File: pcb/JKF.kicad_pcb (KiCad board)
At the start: 2 copper layers, 77.2 x 50.8 mm, 78 parts, among them J1 Conn_01x10_Socket, J10 Conn_01x02_Socket, J11 Conn_01x02_Socket, J12 Conn_01x02_Socket, J13 Conn_01x02_Socket, J14 Conn_01x02_Socket, J15 Conn_01x02_Socket, J16 Conn_01x02_Socket, J17 Conn_01x02_Socket, J18 Conn_01x02_Socket, J19 Conn_01x02_Socket, J2 Conn_01x02_Pin, J20 Conn_01x02_Socket, J21 Conn_01x02_Socket, J22 Conn_01x02_Socket, J23 Conn_01x02_Socket, J24 Conn_01x02_Socket, J25 Conn_01x02_Socket, J26 Conn_01x02_Socket, J27 Conn_01x02_Socket, J28 Conn_01x02_Socket, J29 Conn_01x02_Socket, J3 Conn_01x10_Socket, J30 Conn_01x02_Socket, J31 Conn_01x02_Socket, J32 Conn_01x02_Socket, J33 Conn_01x02_Socket, J34 Conn_01x02_Socket, J35 Conn_01x02_Socket, J36 Conn_01x02_Socket, J37 Conn_01x02_Socket, J4 Conn_02x02_Counter_Clockwise, J5 Conn_02x02_Counter_Clockwise, J6 Conn_02x02_Counter_Clockwise, J7 Conn_02x02_Counter_Clockwise, J8 Conn_02x02_Counter_Clockwise, J9 Conn_02x02_Counter_Clockwise, U1 4027, U2 4027

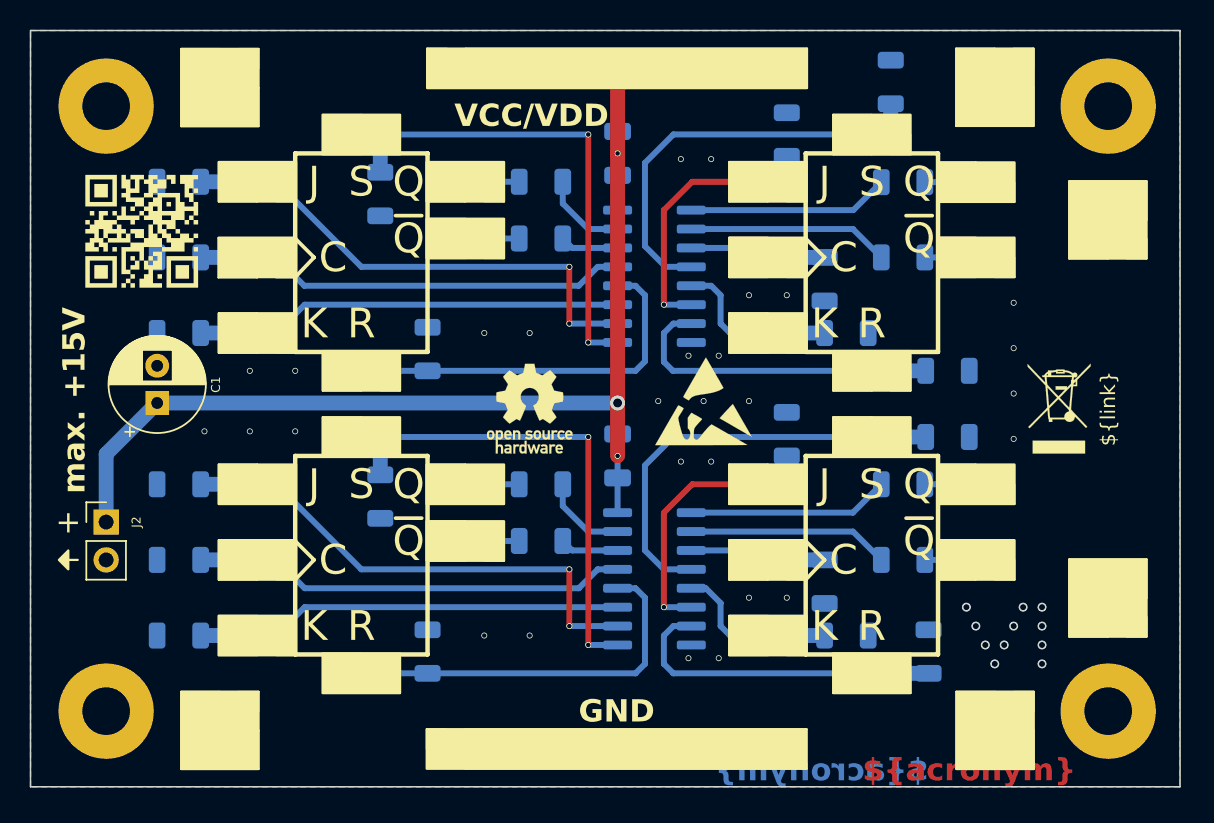
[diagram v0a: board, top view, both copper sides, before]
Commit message: Adapt edge cuts and dimensioning
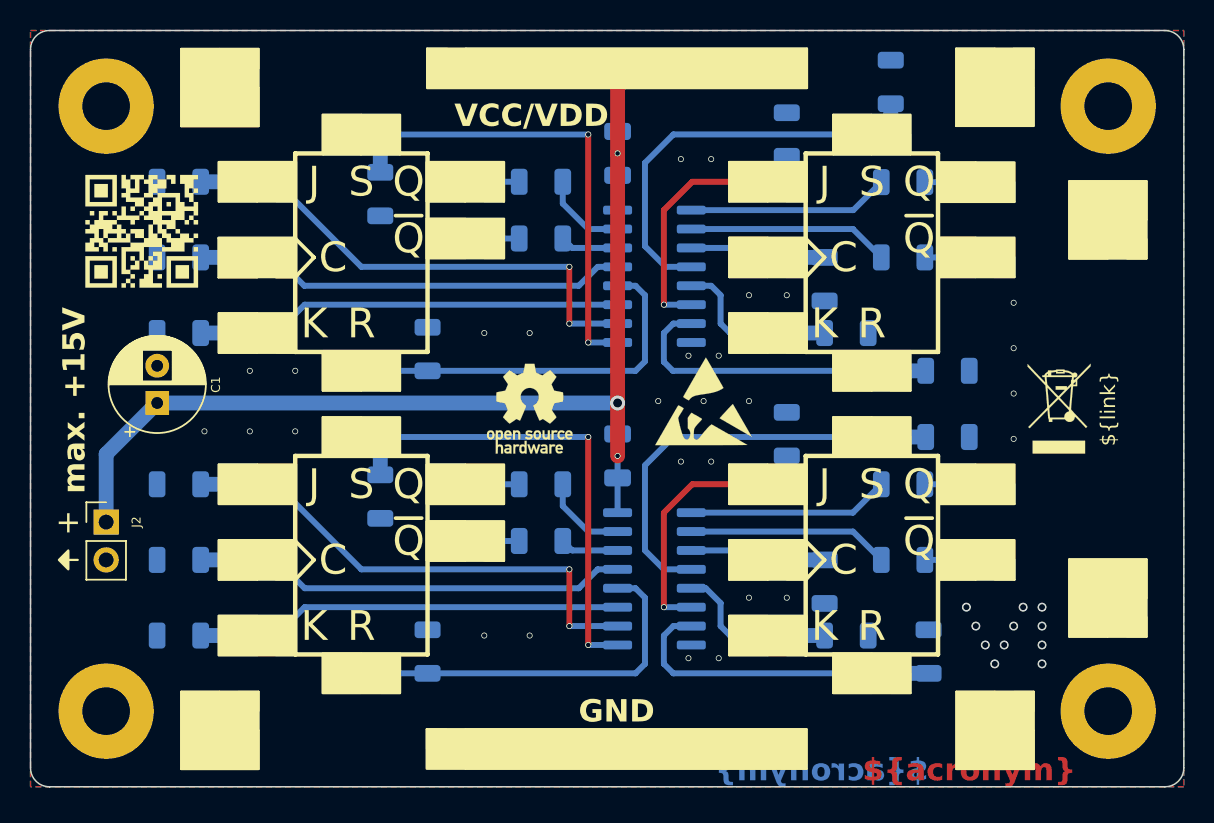
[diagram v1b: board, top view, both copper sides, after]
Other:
- board size 77.2 x 50.8 mm -> 77.5 x 50.8 mm
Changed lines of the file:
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@@
   (gr_rect (start 145.99 105.35) (end 151.19 108.01)
     (stroke (width 0.15) (type solid)) (fill solid) (layer "F.SilkS"))
-  (gr_rect (start 119.38 76.2) (end 196.596 127)
-    (stroke (width 0.1) (type default)) (fill none) (layer "Edge.Cuts"))
+  (gr_line (start 195.58 76.2) (end 120.65 76.2)
+    (stroke (width 0.1) (type default)) (layer "Edge.Cuts"))
+  (gr_line (start 196.85 125.73) (end 196.85 77.47)
+    (stroke (width 0.1) (type default)) (layer "Edge.Cuts"))
+  (gr_line (start 119.38 77.47) (end 119.38 125.73)
+    (stroke (width 0.1) (type default)) (layer "Edge.Cuts"))
+  (gr_arc (start 195.58 76.2) (mid 196.478026 76.571974) (end 196.85 77.47)
+    (stroke (width 0.1) (type default)) (layer "Edge.Cuts"))
+  (gr_arc (start 119.38 77.47) (mid 119.751974 76.571974) (end 120.65 76.2)
+    (stroke (width 0.1) (type default)) (layer "Edge.Cuts"))
+  (gr_line (start 120.65 127) (end 195.58 127)
+    (stroke (width 0.1) (type default)) (layer "Edge.Cuts"))
+  (gr_arc (start 196.85 125.73) (mid 196.478026 126.628026) (end 195.58 127)
+    (stroke (width 0.1) (type default)) (layer "Edge.Cuts"))
+  (gr_arc (start 120.65 127) (mid 119.751974 126.628026) (end 119.38 125.73)
+    (stroke (width 0.1) (type default)) (layer "Edge.Cuts"))
   (gr_text "${acronym}" (at 175.26 126.746) (layer "F.Cu")
     (effects (font (size 1.5 1.5) (thickness 0.3) bold) (justify left bottom))
@@
   (dimension (type aligned) (layer "Dwgs.User")
     (pts (xy 119.38 76.2) (xy 119.38 127))
-    (height 1.27)
-    (gr_text "50.80" (at 116.96 101.6 90) (layer "Dwgs.User")
+    (height 3.81)
+    (gr_text "50.80" (at 114.42 101.6 90) (layer "Dwgs.User")
       (effects (font (size 1 1) (thickness 0.15)))
     )
@@
   )
   (dimension (type aligned) (layer "Dwgs.User")
-    (pts (xy 119.38 76.2) (xy 196.596 76.2))
-    (height -1.27)
-    (gr_text "77.22" (at 157.988 73.78) (layer "Dwgs.User")
+    (pts (xy 119.38 76.2) (xy 196.85 76.2))
+    (height -3.81)
+    (gr_text "77.47" (at 158.115 71.24) (layer "Dwgs.User")
+      (effects (font (size 1 1) (thickness 0.15)))
+    )
+    (format (prefix "") (suffix "") (units 3) (units_format 0) (precision 2))
+    (style (thickness 0.15) (arrow_length 1.27) (text_position_mode 0) (extension_height 0.58642) (extension_offset 0.5) keep_text_aligned)
+  )
+  (dimension (type aligned) (layer "Dwgs.User")
+    (pts (xy 124.46 81.28) (xy 124.46 76.2))
+    (height -6.35)
+    (gr_text "5.08" (at 116.96 78.74 90) (layer "Dwgs.User")
+      (effects (font (size 1 1) (thickness 0.15)))
+    )
+    (format (prefix "") (suffix "") (units 3) (units_format 0) (precision 2))
+    (style (thickness 0.15) (arrow_length 1.27) (text_position_mode 0) (extension_height 0.58642) (extension_offset 0.5) keep_text_aligned)
+  )
+  (dimension (type aligned) (layer "Dwgs.User")
+    (pts (xy 124.46 81.28) (xy 119.38 81.28))
+    (height 6.35)
+    (gr_text "5.08" (at 121.92 73.78) (layer "Dwgs.User")
       (effects (font (size 1 1) (thickness 0.15)))
     )
@@
       (pts
         (xy 119.38 76.2)
-        (xy 196.596 76.2)
-        (xy 196.596 127)
+        (xy 196.85 76.2)
+        (xy 196.85 127)
         (xy 119.38 127)
       )

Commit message: Add reverse polarity protection
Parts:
- added D1: BAT43, Diode_SMD:D_MiniMELF, B.Cu at (139.2, 121.7)
- added D2: BZ5V1, Diode_SMD:D_MiniMELF, B.Cu at (144.5, 123.4)
- added Q1: BUK7880-55A, Package_TO_SOT_SMD:SOT-223-3_TabPin2, B.Cu at (151.8, 119.4)
- added R29: 1k, Resistor_SMD:R_1206_3216Metric, B.Cu at (139.5, 124.0)
- moved R19 13.0 mm to (158.8, 120.8), turned to 90 degrees
- moved R4 2.07 mm to (130.8, 115.4), turned to -90 degrees
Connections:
- J2 pad 2: GND -> Net-(J2-Pin_2)
- J3 pad 1: GND -> Net-(J2-Pin_2)
- J3 pad 10: GND -> Net-(J2-Pin_2)
- J3 pad 2: GND -> Net-(J2-Pin_2)
- J3 pad 3: GND -> Net-(J2-Pin_2)
- J3 pad 4: GND -> Net-(J2-Pin_2)
- J3 pad 5: GND -> Net-(J2-Pin_2)
- J3 pad 6: GND -> Net-(J2-Pin_2)
- J3 pad 7: GND -> Net-(J2-Pin_2)
- J3 pad 8: GND -> Net-(J2-Pin_2)
- J3 pad 9: GND -> Net-(J2-Pin_2)
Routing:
- net Net-(J2-Pin_2): track 0.00 -> 41.9 mm
- net VCC: track 74.5 -> 114.3 mm, vias 3 -> 4
- net Net-(D1-A): track 0.00 -> 9.93 mm
- net Net-(J28-Pin_1): vias 0 -> 1
- net GND: vias 39 -> 47
- added copper zone on B.Cu, net Net-(J2-Pin_2)
